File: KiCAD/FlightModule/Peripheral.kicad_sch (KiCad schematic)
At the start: 13 parts, among them J4 PIN, Q3 2SC3325-Y, U12 MB85RQ8MX, U13 MB85RQ8MX, U14 MB85RQ8MX, U7 TC7S14F

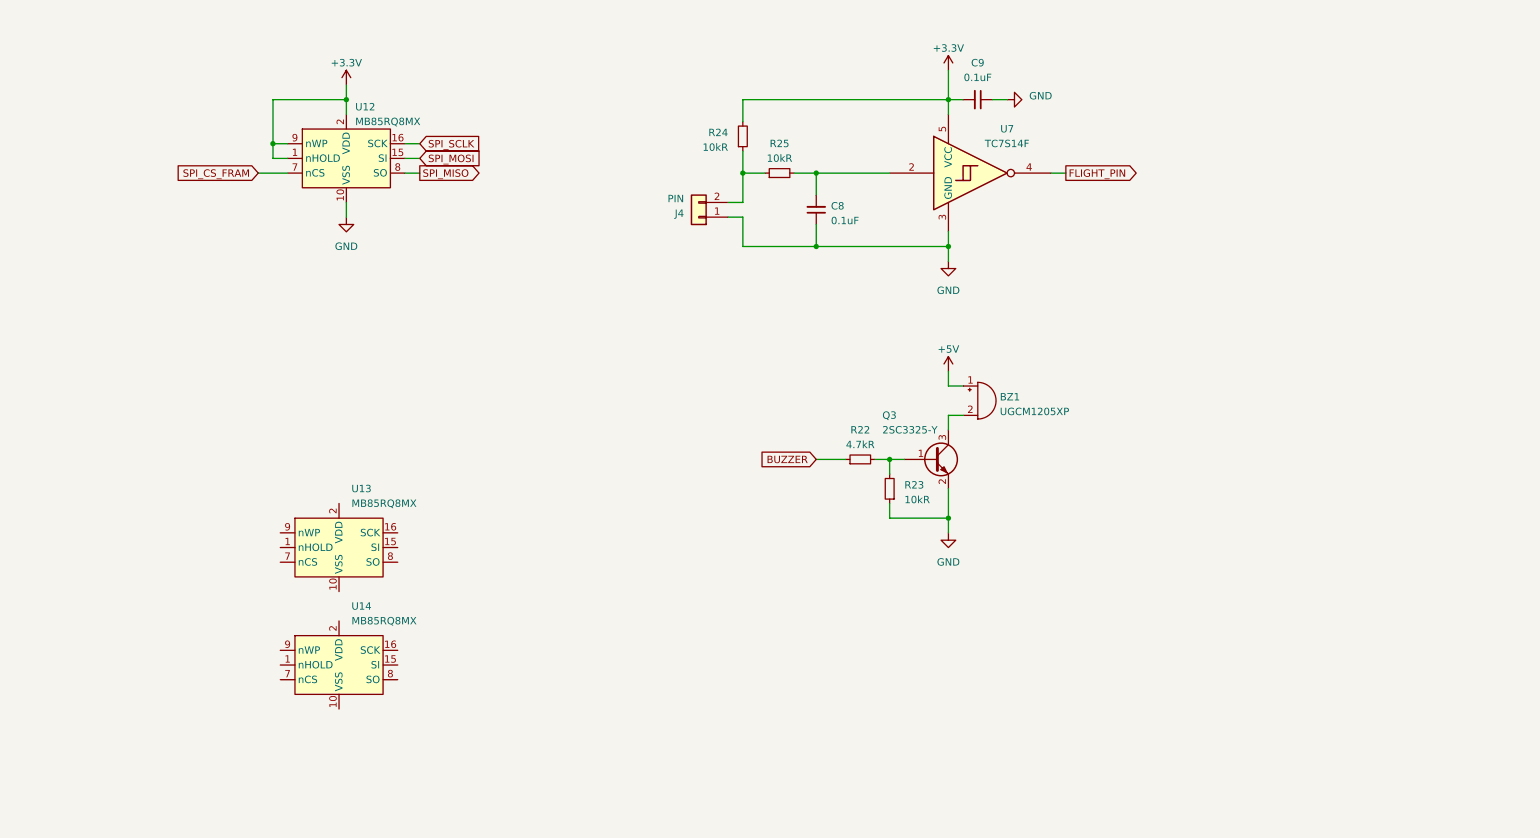
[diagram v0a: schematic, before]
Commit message: M85RQ8MX の回路図完成
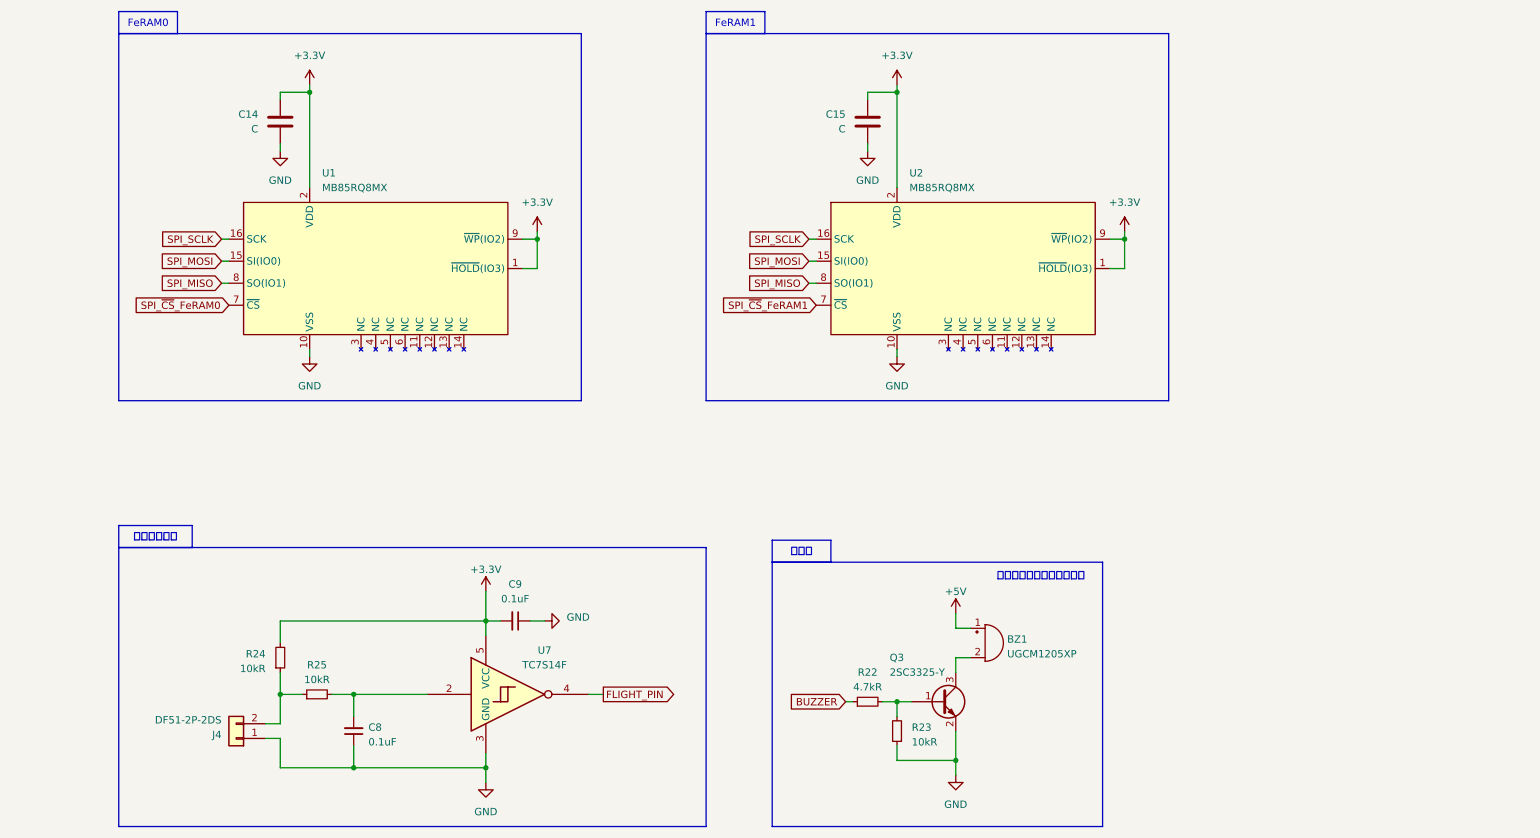
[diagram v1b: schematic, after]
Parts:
- removed U12: MB85RQ8MX, Package_SO:SOIC-16W_7.5x10.3mm_P1.27mm, symbol Memory_NVRAM:MB85RQ8MX
- removed U13, U14: MB85RQ8MX, Package_SO:SOIC-16W_7.5x10.3mm_P1.27mm, symbol TSRP_IC:MB85RQ8MX
- added C14, C15: C, symbol Device:C
- added U1, U2: MB85RQ8MX, Package_SO:SOIC-16W_7.5x10.3mm_P1.27mm, symbol TSRP_IC:MB85RQ8MX
- J4: value PIN -> DF51-2P-2DS; footprint Hirose_Connector:Hirose_DF1B -> TSRP_Connector_Hirose:DF51-2P-2DS
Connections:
- net +3.3V: now also C14.1, C15.1, U1.1 (~{HOLD}(IO3)), U1.2 (VDD), U1.9 (~{WP}(IO2)), U2.1 (~{HOLD}(IO3)), U2.2 (VDD), U2.9 (~{WP}(IO2))
- net GND: now also C14.2, C15.2, U1.10 (VSS), U2.10 (VSS)
- net SPI_MISO: now also U1.8 (SO(IO1)), U2.8 (SO(IO1))
- net SPI_MOSI: now also U1.15 (SI(IO0)), U2.15 (SI(IO0))
- net SPI_SCLK: now also U1.16 (SCK), U2.16 (SCK)
- new net SPI_~{CS}_FeRAM0: U1.7 (~{CS})
- new net SPI_~{CS}_FeRAM1: U2.7 (~{CS})
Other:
- note added: "現在の状態を把握するため"
- moved on the sheet: BZ1, C8, C9, J4, Q3, R22, R23, R24, R25, U7

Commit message: 配線8割り終わり．次の作業....
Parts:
- BZ1, Q3, R22, R23: now not fitted; now left out of the parts list
- C14, C15: value C -> 0.1uF; footprint (none) -> Capacitor_SMD:C_0603_1608Metric_Pad1.08x0.95mm_HandSolder
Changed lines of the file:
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@@
 		(at 168.91 142.24 180)
 		(unit 1)
-		(exclude_from_sim no)
-		(in_bom yes)
-		(on_board yes)
-		(dnp no)
+		(exclude_from_sim yes)
+		(in_bom no)
+		(on_board no)
+		(dnp yes)
 		(fields_autoplaced yes)
 		(property "Reference" "R23"
@@
 		(at 184.15 127 0)
 		(unit 1)
-		(exclude_from_sim no)
-		(in_bom yes)
-		(on_board yes)
-		(dnp no)
+		(exclude_from_sim yes)
+		(in_bom no)
+		(on_board no)
+		(dnp yes)
 		(fields_autoplaced yes)
 		(property "Reference" "BZ1"
@@
 		(at 163.83 137.16 90)
 		(unit 1)
-		(exclude_from_sim no)
-		(in_bom yes)
-		(on_board yes)
-		(dnp no)
+		(exclude_from_sim yes)
+		(in_bom no)
+		(on_board no)
+		(dnp yes)
 		(fields_autoplaced yes)
 		(property "Reference" "R22"
@@
 		(at 176.53 137.16 0)
 		(unit 1)
-		(exclude_from_sim no)
-		(in_bom yes)
-		(on_board yes)
-		(dnp no)
+		(exclude_from_sim yes)
+		(in_bom no)
+		(on_board no)
+		(dnp yes)
 		(property "Reference" "Q3"
 			(at 167.64 129.54 0)
@@
 			)
 		)
-		(property "Value" "C"
+		(property "Value" "0.1uF"
 			(at 58.42 38.0999 0)
 			(effects
@@
 			)
 		)
-		(property "Footprint" ""
+		(property "Footprint" "Capacitor_SMD:C_0603_1608Metric_Pad1.08x0.95mm_HandSolder"
 			(at 61.2648 40.64 0)
 			(effects
@@
 			)
 		)
-		(property "Value" "C"
+		(property "Value" "0.1uF"
 			(at 160.02 38.0999 0)
 			(effects
@@
 			)
 		)
-		(property "Footprint" ""
+		(property "Footprint" "Capacitor_SMD:C_0603_1608Metric_Pad1.08x0.95mm_HandSolder"
 			(at 162.8648 40.64 0)
 			(effects

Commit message: FeRAMを3個に増設
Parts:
- added C18: 0.1uF, Capacitor_SMD:C_0603_1608Metric_Pad1.08x0.95mm_HandSolder, symbol Device:C
- added U4: MB85RQ8MX, Package_SO:SOIC-16W_7.5x10.3mm_P1.27mm, symbol TSRP_IC:MB85RQ8MX
- BZ1, Q3, R22, R23: now fitted; now in the parts list
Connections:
- net +3.3V: now also C18.1, U4.1 (~{HOLD}(IO3)), U4.2 (VDD), U4.9 (~{WP}(IO2))
- net GND: now also C18.2, U4.10 (VSS)
- net SPI_MISO: now also U4.8 (SO(IO1))
- net SPI_MOSI: now also U4.15 (SI(IO0))
- net SPI_SCLK: now also U4.16 (SCK)
- new net SPI_~{CS}_FeRAM2: U4.7 (~{CS})
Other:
- moved on the sheet: C14, C15, C8, C9, J4, R24, R25, U1, U2, U7
